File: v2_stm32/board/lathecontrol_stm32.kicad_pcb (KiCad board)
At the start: 2 copper layers, 73 parts, among them IC1 LM393, IC2 LM393, IC3 LM393, IC4 LM393, J1 Conn_01x05_Male, J10 USB_A, J11 USB_A, J12 USB_A, J13 Conn_01x04_Male, J2 Conn_01x05_Male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

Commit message: More routing
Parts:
- moved U3 105.8 mm to (218.2, 140.3), turned to 270 degrees
- moved D5 98.6 mm to (216.5, 131.9), turned to 90 degrees
- moved R20 92.2 mm to (220.8, 132.7)
- moved R21 89.3 mm to (221.6, 129.5), turned to 90 degrees
- moved C19 85.9 mm to (219.1, 129.2), turned to 90 degrees
- moved C18 84.9 mm to (215.4, 128.3)
- moved R24 81.8 mm to (72.4, 124.5), turned to 90 degrees
- moved U5 80.1 mm to (77.5, 129.5), turned to 0 degrees
- moved C22 80.0 mm to (71.3, 130.8), turned to 0 degrees
- moved J13 80.0 mm to (78.1, 134.0)
- moved R23 79.1 mm to (69.8, 126.4)
- moved Q1 77.3 mm to (75.6, 124.5), turned to 0 degrees
- moved C1 50.0 mm to (132.7, 66.0)
- moved U4 47.4 mm to (155.0, 166.4), turned to 90 degrees
- moved C21 47.2 mm to (162.6, 163.8), turned to 270 degrees
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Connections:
- net Net-(C15-Pad2) renamed /Power/5VRAW
- J13 pad 1: /Rotation Input/ROTIN_PWR -> /Rotation Input/ROTIN_GND
- J13 pad 2: /Rotation Input/ROTIN_DAT -> Net-(J13-Pad2)
- J13 pad 3: Net-(J13-Pad3) -> /Rotation Input/ROTIN_DAT
- J13 pad 4: /Rotation Input/ROTIN_GND -> /Rotation Input/ROTIN_PWR
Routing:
- net GND: track 185.5 -> 253.0 mm, vias 8 -> 13
- net +5V: track 0.00 -> 41.3 mm
- net Net-(C16-Pad1): track 0.00 -> 23.2 mm
- net +1V8: track 56.5 -> 76.3 mm
- net /Rotation Input/ROTIN_GND: track 0.00 -> 15.0 mm, vias 0 -> 1
- net VCC: track 0.00 -> 12.1 mm
- net /Power/5VRAW: track 0.00 -> 11.9 mm
- net Net-(Q1-Pad3): track 0.00 -> 11.3 mm
- net /Rotation Input/ROTIN_PWR: track 0.00 -> 10.0 mm, vias 0 -> 1
- net /Rotation Input/ROTIN_DAT: track 0.00 -> 8.96 mm, vias 0 -> 1
- net /Power/VADJ_1V8: track 0.00 -> 7.60 mm
- net Net-(R13-Pad2): track 0.00 -> 6.53 mm
- net Net-(R23-Pad1): track 0.00 -> 6.36 mm
- net /OSC_OUT: track 0.00 -> 3.52 mm
- net /OSC_IN: track 0.00 -> 3.52 mm
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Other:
- net class Power: clearance 0.5 -> 0.2

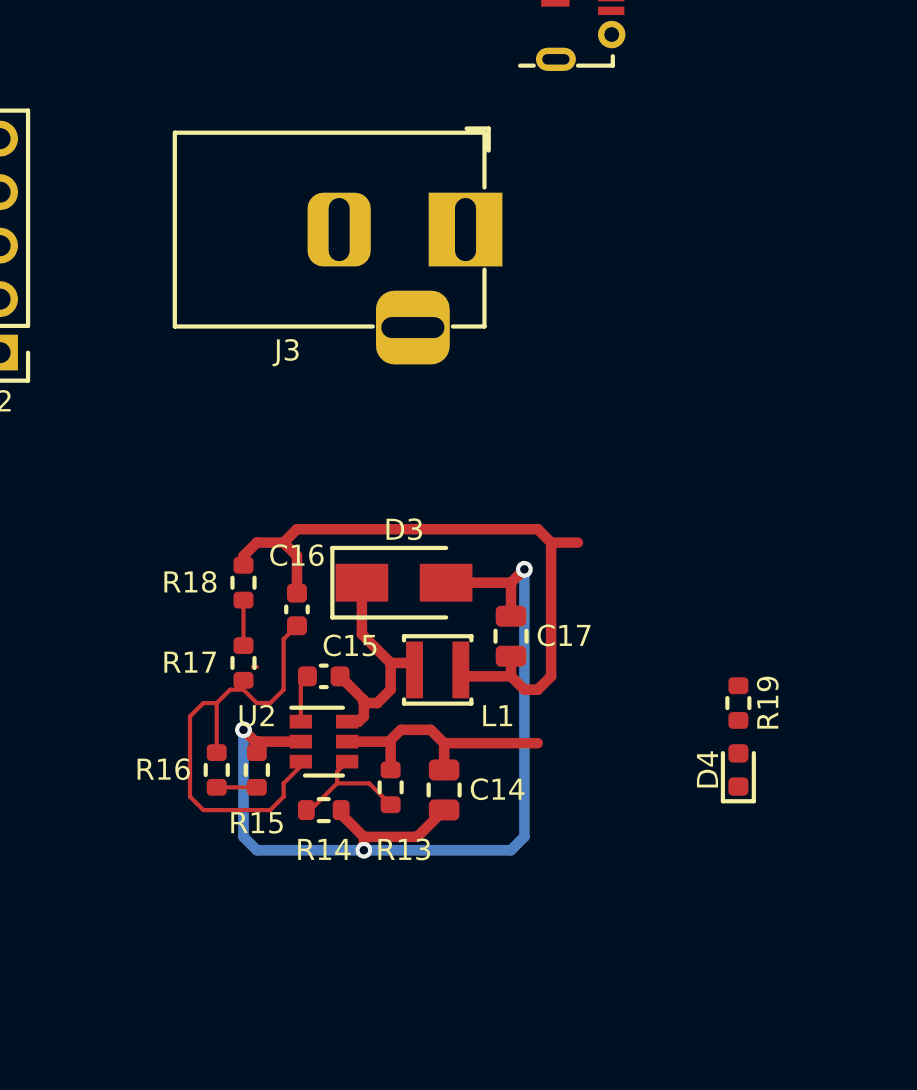
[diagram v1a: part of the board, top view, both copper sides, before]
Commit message: MP2451 Routing according to datasheet
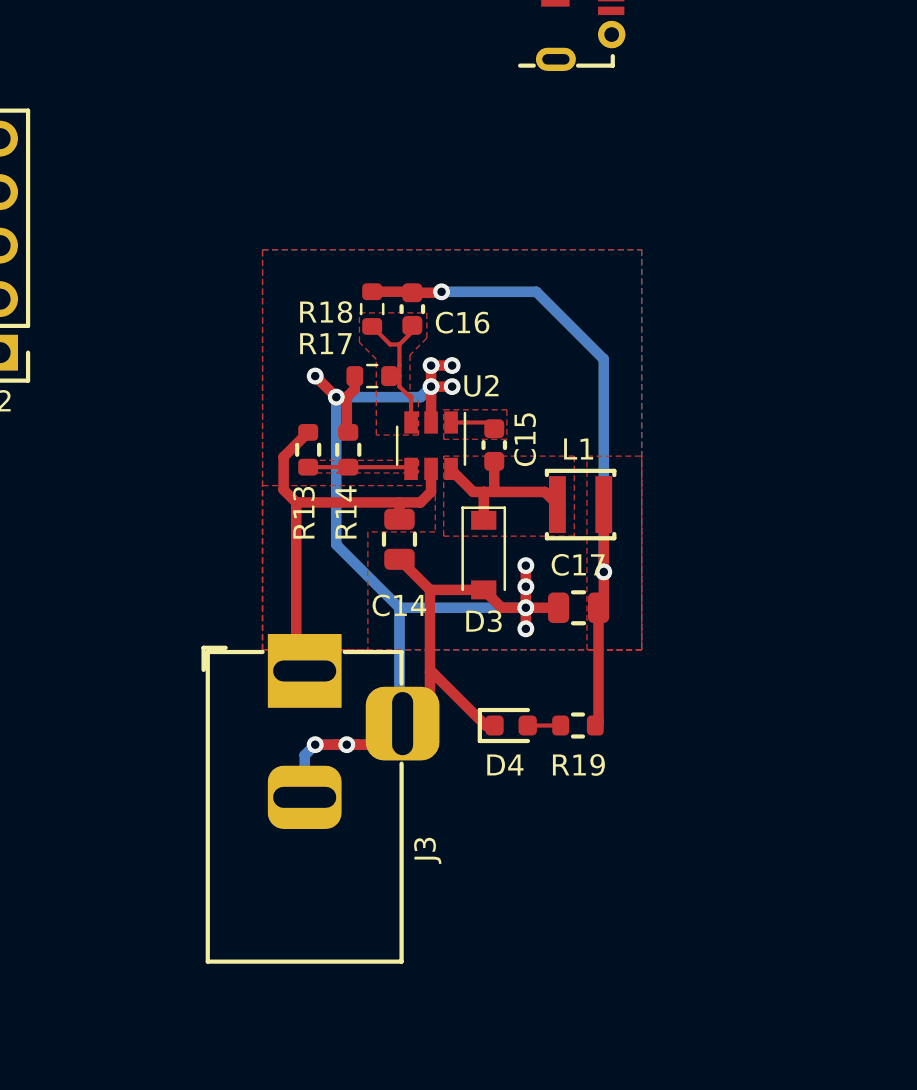
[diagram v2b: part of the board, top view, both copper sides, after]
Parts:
- removed R15: 5k6, Resistor_SMD:R_0603_1608Metric
- removed R16: 18k, Resistor_SMD:R_0603_1608Metric
- D3: footprint Diode_SMD:D_SMA -> Diode_SMD:D_SOD-123
- R18: value 100k -> 120k
- moved J3 22.3 mm to (128.0, 135.0), turned to 90 degrees
- moved R14 17.1 mm to (130.1, 124.5), turned to 270 degrees
- moved R13 16.5 mm to (128.2, 124.5)
- moved C16 15.3 mm to (133.1, 117.8)
- moved U2 14.9 mm to (134.0, 124.3), turned to 270 degrees
- moved R17 14.9 mm to (131.2, 121.0), turned to 0 degrees
- moved R18 14.4 mm to (131.2, 117.8)
- moved C15 13.6 mm to (137.0, 124.3), turned to 270 degrees
- moved C14 12.1 mm to (132.5, 128.8)
- moved D4 11.0 mm to (137.8, 137.6), turned to 0 degrees
- moved L1 10.4 mm to (139.5, 125.5)
- moved R19 7.69 mm to (141.0, 137.6), turned to 180 degrees
- moved D3 4.01 mm to (136.5, 129.5), turned to 270 degrees
- moved C17 3.48 mm to (141.0, 132.0), turned to 180 degrees
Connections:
- net /Power/5VRAW renamed /Power/5VSW
- net Net-(C15-Pad1) renamed /Power/5VBST
- net Net-(R13-Pad2) renamed /Power/5VEN
- C16 pad 1: Net-(C16-Pad1) -> /Power/5VFB
- R17 pad 1: Net-(C16-Pad1) -> GND
- R17 pad 2: Net-(R17-Pad2) -> /Power/5VFB
- R18 pad 1: Net-(R17-Pad2) -> /Power/5VFB
- U2 pad 3: Net-(C16-Pad1) -> /Power/5VFB
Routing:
- net GND: track 253.0 -> 277.9 mm, vias 13 -> 22
- net Net-(C16-Pad1): track 23.2 -> 0.00 mm
- net VCC: track 12.1 -> 20.9 mm
- net /Power/5VFB: track 0.00 -> 7.22 mm
- net /Power/5VSW: track 11.9 -> 8.58 mm
- net Net-(R17-Pad2): track 2.16 -> 0.00 mm
- net Net-(R15-Pad2): track 1.91 -> 0.00 mm
- net /Power/5VEN: track 6.53 -> 4.92 mm
- net Net-(D4-Pad2): track 0.00 -> 1.56 mm
- net +5V: track 41.3 -> 42.4 mm, vias 0 -> 2
- added copper zone on F.Cu, net +5V
- added copper zone on F.Cu, net /Power/5VBST
- added copper zone on F.Cu, net /Power/5VEN
- added copper zone on F.Cu, net /Power/5VFB
- added copper zone on F.Cu, net /Power/5VSW
- added copper zone on B.Cu, net GND
- added copper zone on F.Cu, net GND
- added copper zone on F.Cu, net VCC

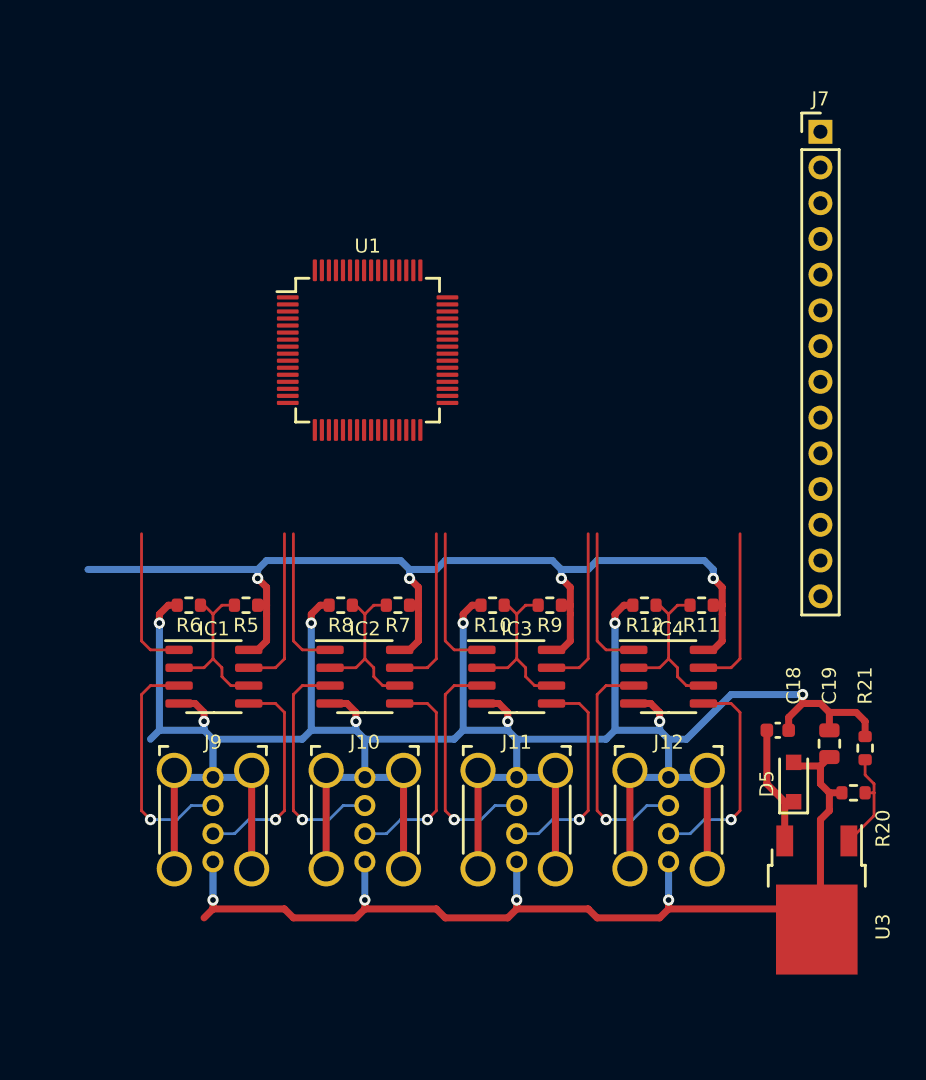
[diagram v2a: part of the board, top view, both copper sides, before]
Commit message: Optimized measuring stick input
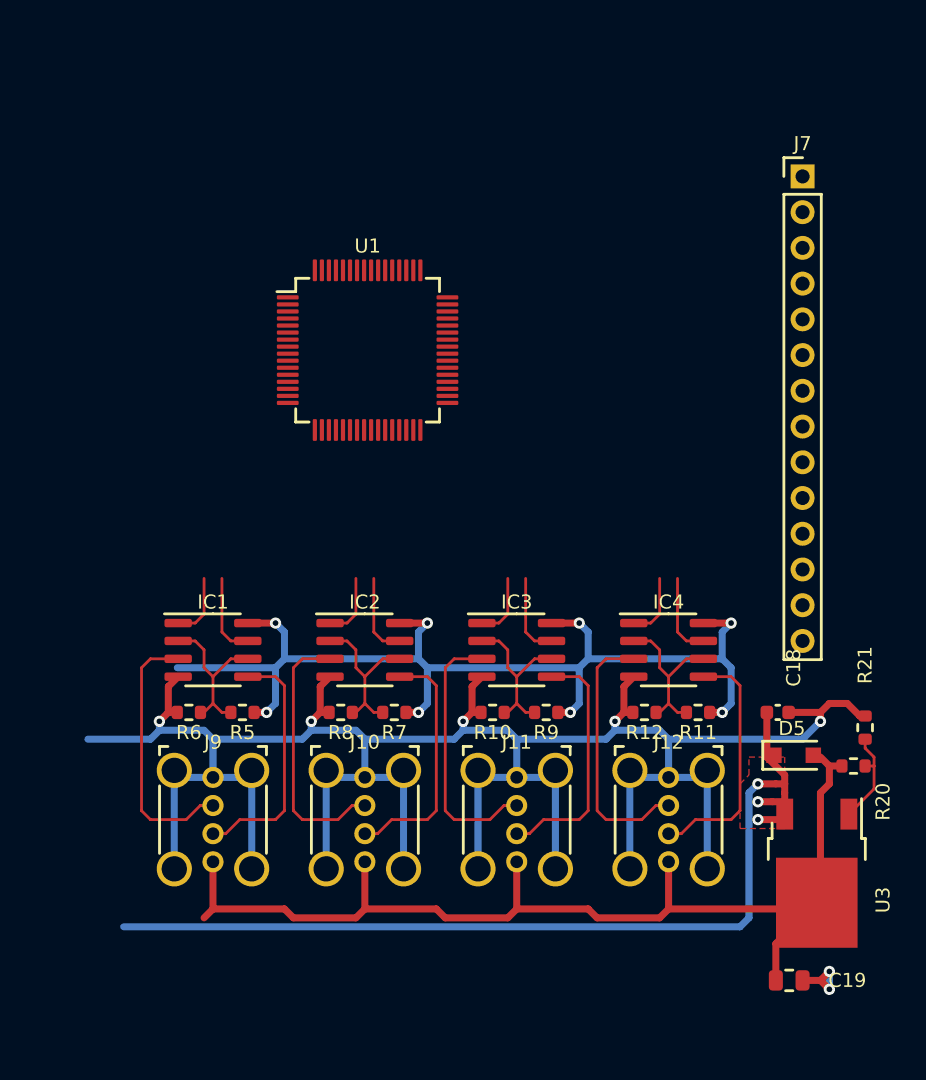
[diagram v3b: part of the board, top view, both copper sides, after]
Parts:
- moved C19 17.1 mm to (216.2, 146.1), turned to 0 degrees
- moved R11 7.62 mm to (209.7, 127.0)
- moved R5 7.62 mm to (177.4, 127.0)
- moved R7 7.62 mm to (188.2, 127.0)
- moved R9 7.62 mm to (198.9, 127.0)
- moved R10 7.62 mm to (195.1, 127.0)
- moved R12 7.62 mm to (205.9, 127.0)
- moved R6 7.62 mm to (173.5, 127.0)
- moved R8 7.62 mm to (184.3, 127.0)
- moved J7 3.42 mm to (217.2, 88.9)
- moved IC1 1.91 mm to (175.3, 122.6)
- moved D5 1.91 mm to (216.5, 130.0), turned to 0 degrees
- moved R20 1.91 mm to (220.8, 130.8)
- moved U3 1.91 mm to (218.2, 138.4)
- moved IC2 1.90 mm to (186.1, 122.6)
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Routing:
- net +5V: track 42.4 -> 101.5 mm, vias 2 -> 5
- net GND: track 277.9 -> 252.0 mm, vias 22 -> 20
- net MS2_DAT: track 10.6 -> 4.64 mm
- net MS4_DAT: track 10.6 -> 4.64 mm
- net MS3_DAT: track 10.6 -> 4.64 mm
- net MS1_DAT: track 10.6 -> 4.64 mm
- net MS3_CLK: track 11.7 -> 5.91 mm
- net MS4_CLK: track 11.7 -> 5.91 mm
- net MS2_CLK: track 11.7 -> 5.91 mm
- net MS1_CLK: track 11.7 -> 5.91 mm
- net +1V8: track 76.3 -> 78.5 mm, vias 4 -> 0
- net /Measurestick Input 4/IN_Clk: track 15.5 -> 17.5 mm, vias 1 -> 0
- net /Measurestick Input 3/IN_Clk: track 15.5 -> 17.5 mm, vias 1 -> 0
- net /Measurestick Input 2/IN_Clk: track 15.5 -> 17.5 mm, vias 1 -> 0
- net /Measurestick Input 1/IN_Clk: track 15.5 -> 17.5 mm, vias 1 -> 0
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
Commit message: More PCB design
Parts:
- removed C17: 22u, Capacitor_SMD:C_0805_2012Metric
- removed D1: RED, LED_SMD:LED_0603_1608Metric
- removed J2: Conn_01x05_Male, Connector_PinHeader_2.54mm:PinHeader_1x05_P2.54mm_Vertical
- removed R2: 240, Resistor_SMD:R_0603_1608Metric
- added C10: 10u, Capacitor_SMD:C_0805_2012Metric, F.Cu at (157.2, 117.5)
- added C11: 10u, Capacitor_SMD:C_0805_2012Metric, F.Cu at (157.2, 120.5)
- added D7: D_Schottky, Diode_SMD:D_SOD-123, F.Cu at (148.7, 121.5)
- added FB1: 600 @ 600MHz, Inductor_SMD:L_0805_2012Metric, F.Cu at (144.0, 119.8)
- added H1: MountingHole_Pad, MountingHole:MountingHole_3mm_Pad, F.Cu at (137.0, 71.0)
- added H2: MountingHole_Pad, MountingHole:MountingHole_3mm_Pad, F.Cu at (137.0, 120.5)
- added H3: MountingHole_Pad, MountingHole:MountingHole_3mm_Pad, F.Cu at (229.0, 120.5)
- added H4: MountingHole_Pad, MountingHole:MountingHole_3mm_Pad, F.Cu at (229.0, 71.0)
- added H5: MountingHole_Pad, MountingHole:MountingHole_3mm_Pad, F.Cu at (229.0, 143.0)
- added H6: MountingHole_Pad, MountingHole:MountingHole_3mm_Pad, F.Cu at (137.0, 143.0)
- added JP1: BOOTSEL, Connector_PinHeader_2.54mm:PinHeader_1x02_P2.54mm_Horizontal, F.Cu at (144.8, 78.0)
- added L2: 39n, Inductor_SMD:L_0402_1005Metric, F.Cu at (177.5, 95.2)
- added Q2: AO3401A, Package_TO_SOT_SMD:SOT-23, F.Cu at (147.9, 125.2)
- added Q3: AO3401A, Package_TO_SOT_SMD:SOT-23, F.Cu at (157.5, 128.0)
- C8: value 100n -> 1u; footprint Capacitor_SMD:C_0603_1608Metric -> Inductor_SMD:L_0402_1005Metric
- C9: value 100n -> 10n; footprint Capacitor_SMD:C_0603_1608Metric -> Inductor_SMD:L_0402_1005Metric
- J1: value Conn_01x05_Male -> Conn_01x06_Male; footprint Connector_PinHeader_2.54mm:PinHeader_1x05_P2.54mm_Vertical -> Connector_PinHeader_2.54mm:PinHeader_1x06_P2.54mm_Vertical
- J5: footprint Connector_PinHeader_2.54mm:PinHeader_1x05_P2.54mm_Vertical -> Connector_PinHeader_2.54mm:PinHeader_1x06_P2.54mm_Horizontal
- J6: footprint Connector_PinHeader_2.54mm:PinHeader_1x05_P2.54mm_Vertical -> Connector_PinHeader_2.54mm:PinHeader_1x05_P2.54mm_Horizontal
- J7: footprint Connector_PinHeader_2.54mm:PinHeader_1x14_P2.54mm_Vertical -> Connector_PinSocket_2.54mm:PinSocket_1x14_P2.54mm_Vertical
- moved J6 106.6 mm to (209.2, 78.0), turned to 90 degrees
- moved J1 103.8 mm to (167.0, 140.0), turned to 180 degrees
- moved C22 101.9 mm to (160.2, 81.2), turned to 180 degrees
- moved R23 100.4 mm to (161.7, 85.6), turned to 90 degrees
- moved R24 94.3 mm to (159.1, 87.5), turned to 270 degrees
- moved J13 93.8 mm to (153.4, 78.0), turned to 90 degrees
- moved C8 93.1 mm to (176.8, 97.5), turned to 270 degrees
- moved U5 89.9 mm to (154.0, 82.5), turned to 180 degrees
- moved J5 89.8 mm to (187.8, 78.0), turned to 90 degrees
- moved Q1 88.4 mm to (155.9, 87.5), turned to 180 degrees
- moved D2 84.0 mm to (172.0, 100.0)
- moved C2 82.7 mm to (192.2, 100.2)
- moved D6 80.9 mm to (143.8, 89.8)
- moved C4 78.9 mm to (182.5, 102.0), turned to 180 degrees
- moved C7 77.0 mm to (194.0, 88.8)
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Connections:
- net BOOT0 renamed /BOOT0
- C8 pad 1: +3V3 -> +3.3VA
- C9 pad 1: +5V -> +3.3VA
- D2 pad 1: /LED_STAT1 -> GND
- J1 pad 1: GND -> IN_+5V
- J1 pad 2: SPI_SCK -> SWCLK
- J1 pad 3: SWCLK -> GND
- J1 pad 5: +3V3 -> NRST
- J3 pad 1: VCC -> IN_VCC
- J4 pad 1: +5V -> IN_+5V
- J5 pad 2: BTN4 -> BTN1
- J5 pad 3: BTN3 -> BTN2
- J5 pad 4: BTN2 -> BTN3
- J5 pad 5: BTN1 -> BTN4
- J6 pad 2: +5V -> +3V3
- J7 pad 7: +5V -> DISPL_LED
- J8 pad 13: GPIO1 -> Net-(J8-Pad13)
- J8 pad 14: GPIO2 -> Net-(J8-Pad14)
- J8 pad 2: SPI_SCK -> Net-(J8-Pad2)
- J8 pad 3: SPI_MISO -> Net-(J8-Pad3)
- J8 pad 4: SPI_MOSI -> Net-(J8-Pad4)
- J8 pad 5: SPI_SS0 -> Net-(J8-Pad5)
- J8 pad 6: SPI_SS1 -> Net-(J8-Pad6)
- R4 pad 1: +3V3 -> /LED_STAT1
- U1 pad 13: +3V3 -> +3.3VA
- U1 pad 14: /LED_STAT0 -> Net-(U1-Pad14)
- U1 pad 29: UART_TX -> DISPL_LED
- U1 pad 3: GPIO1 -> Net-(U1-Pad3)
- U1 pad 30: UART_RX -> DISPL_T_IRQ
- U1 pad 33: DISPL_T_IRQ -> Net-(U1-Pad33)
- U1 pad 4: GPIO2 -> Net-(U1-Pad4)
- U1 pad 50: BTN4 -> Net-(U1-Pad50)
- U1 pad 51: BTN3 -> BTN4
- U1 pad 52: BTN2 -> BTN3
- U1 pad 53: BTN1 -> Net-(U1-Pad53)
- U1 pad 55: SPI_SCK -> SWD_SWO
- U1 pad 56: SPI_MISO -> BTN2
- U1 pad 57: SPI_MOSI -> BTN1
- U1 pad 58: SPI_SS0 -> UART_TX
- U1 pad 59: SPI_SS1 -> UART_RX
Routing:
- net USB_D+: track 0.00 -> 91.9 mm, vias 0 -> 4
- net USB_D-: track 0.00 -> 90.0 mm, vias 0 -> 4
- net +3V3: track 76.8 -> 165.8 mm, vias 8 -> 12
- net +5V: track 101.5 -> 175.3 mm, vias 5 -> 10
- net SWD_SWO: track 0.00 -> 63.4 mm
- net SWCLK: track 0.00 -> 63.2 mm, vias 0 -> 2
- net SWDIO: track 0.00 -> 57.6 mm, vias 0 -> 2
- net GND: track 252.0 -> 308.0 mm, vias 20 -> 62
- net NRST: track 0.00 -> 48.2 mm
- net ADC2: track 0.00 -> 37.9 mm, vias 0 -> 2
- net ADC3: track 0.00 -> 37.7 mm, vias 0 -> 2
- net ADC1: track 0.00 -> 36.8 mm, vias 0 -> 2
- net ADC4: track 0.00 -> 36.4 mm, vias 0 -> 2
- net MS4_DAT: track 4.64 -> 40.5 mm
- net MS4_CLK: track 5.91 -> 40.9 mm
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- added copper zone on F.Cu, net +1V8
- added copper zone on F.Cu, net +3.3VA
- added copper zone on F.Cu, net +3V3
- added copper zone on F.Cu, net /Power/VADJ_1V8
- added copper zone on F.Cu, net /Power/VCC_MID
- added copper zone on F.Cu, net IN_VCC
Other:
- board outline added: 99 x 79 mm
- net class Default: trace_width 0.2 -> 0.3
- net class USB added: clearance 0.1, trace_width 0.3, via_dia 0.8, via_drill 0.4
- board text added: "LED_STAT"
